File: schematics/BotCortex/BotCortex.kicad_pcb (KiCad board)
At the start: 2 copper layers, 59 parts, among them P1 2x Serial, P10 Stepper Upperarm, P11 Stepper Hip, P12 POWER_IN, P13 PowerEnableIn, P14 Power Stepper 2, P15 Power Stepper 3, P16 Power Stepper 4, P17 PowerEnableOut, P18 Power Stepper 5, P19 ODroid Power, P2 Herkulex Servo, P20 POTI 10K, P21 Reset_Conn, P22 Reset Conn, P23 LED-Driver-I2C, P24 UART6, P25 Thermal_Printer, P28 Power Stepper 1, P3 Encoder Socket 0, P4 Encoder Socket, P5 Stepper Elbow, P6 Power In uC Servo 9V, P7 Power Out uC Servo, P8 Stepper Forearm, P9 Stepper Wrist, Q1 BC237, Q2 BC237, SW2 reset, U1 7805, U2 LM7809ACT, U3 LM7809ACT, U4 Teensy_3.5

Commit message: Started Implementation of Webserver for Odroid
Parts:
- added P26: ResetTaster, Connectors_Molex:Molex_KK_6410-02, F.Cu at (125.7, 68.6)
- moved P21 1.27 mm to (138.4, 68.6)
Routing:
- net Net-(P21-Pad1): track 3.81 -> 14.0 mm
- net GNDPWR: track 709.1 -> 716.7 mm
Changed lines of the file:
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@@
 (kicad_pcb (version 4) (host pcbnew 4.0.2-stable)
   (general
-    (links 136)
+    (links 138)
     (no_connects 14)
     (area 0 0 0 0)
     (thickness 1.6)
     (drawings 4)
-    (tracks 407)
+    (tracks 409)
     (zones 0)
-    (modules 59)
+    (modules 60)
     (nets 53)
   )
@@
   )
   (module Connect:1pin (layer F.Cu)
-    (at 138.43 69.85)
+    (at 138.43 68.58)
     (descr "module 1 pin (ou trou mecanique de percage)")
     (tags DEV)
@@
     )
   )
+  (module Connectors_Molex:Molex_KK_6410-02 (layer F.Cu)
+    (at 125.73 68.58)
+    (descr "Connector Headers with Friction Lock, 22-27-2021, http://www.molex.com/pdm_docs/sd/022272021_sd.pdf")
+    (tags "connector molex kk_6410 22-27-2021")
+    (fp_text reference P26 (at 1 -4.5) (layer F.SilkS)
+      (effects (font (size 1 1) (thickness 0.15)))
+    )
+    (fp_text value ResetTaster (at 1.27 4.5) (layer F.Fab)
+      (effects (font (size 1 1) (thickness 0.15)))
+    )
+    (fp_line (start -1.37 -3.02) (end -1.37 2.98) (layer F.SilkS) (width 0.15))
+    (fp_line (start -1.37 2.98) (end 3.91 2.98) (layer F.SilkS) (width 0.15))
+    (fp_line (start 3.91 2.98) (end 3.91 -3.02) (layer F.SilkS) (width 0.15))
+    (fp_line (start 3.91 -3.02) (end -1.37 -3.02) (layer F.SilkS) (width 0.15))
+    (fp_line (start 0 2.98) (end 0 1.98) (layer F.SilkS) (width 0.15))
+    (fp_line (start 0 1.98) (end 2.54 1.98) (layer F.SilkS) (width 0.15))
+    (fp_line (start 2.54 1.98) (end 2.54 2.98) (layer F.SilkS) (width 0.15))
+    (fp_line (start 0 1.98) (end 0.25 1.55) (layer F.SilkS) (width 0.15))
+    (fp_line (start 0.25 1.55) (end 2.29 1.55) (layer F.SilkS) (width 0.15))
+    (fp_line (start 2.29 1.55) (end 2.54 1.98) (layer F.SilkS) (width 0.15))
+    (fp_line (start 0.25 2.98) (end 0.25 1.98) (layer F.SilkS) (width 0.15))
+    (fp_line (start 2.29 2.98) (end 2.29 1.98) (layer F.SilkS) (width 0.15))
+    (fp_line (start -0.8 -3.02) (end -0.8 -2.4) (layer F.SilkS) (width 0.15))
+    (fp_line (start -0.8 -2.4) (end 0.8 -2.4) (layer F.SilkS) (width 0.15))
+    (fp_line (start 0.8 -2.4) (end 0.8 -3.02) (layer F.SilkS) (width 0.15))
+    (fp_line (start 1.74 -3.02) (end 1.74 -2.4) (layer F.SilkS) (width 0.15))
+    (fp_line (start 1.74 -2.4) (end 3.34 -2.4) (layer F.SilkS) (width 0.15))
+    (fp_line (start 3.34 -2.4) (end 3.34 -3.02) (layer F.SilkS) (width 0.15))
+    (fp_line (start -1.9 3.5) (end -1.9 -3.55) (layer F.CrtYd) (width 0.05))
+    (fp_line (start -1.9 -3.55) (end 4.45 -3.55) (layer F.CrtYd) (width 0.05))
+    (fp_line (start 4.45 -3.55) (end 4.45 3.5) (layer F.CrtYd) (width 0.05))
+    (fp_line (start 4.45 3.5) (end -1.9 3.5) (layer F.CrtYd) (width 0.05))
+    (pad 1 thru_hole rect (at 0 0) (size 2 2.6) (drill 1.2) (layers *.Cu *.Mask F.SilkS)
+      (net 2 GNDPWR))
+    (pad 2 thru_hole oval (at 2.54 0) (size 2 2.6) (drill 1.2) (layers *.Cu *.Mask F.SilkS)
+      (net 44 "Net-(P21-Pad1)"))
+  )
   (target plus (at 91.44 33.02) (size 5) (width 0.1) (layer Edge.Cuts))
   (target plus (at 109.22 125.73) (size 5) (width 0.1) (layer Edge.Cuts))
@@
   (segment (start 182.88 76.2) (end 196.85 76.2) (width 0.25) (layer B.Cu) (net 1) (status 10))
   (segment (start 198.12 73.66) (end 198.12 73.66) (width 0.25) (layer B.Cu) (net 1) (status 30))
+  (segment (start 125.73 68.58) (end 118.11 68.58) (width 0.25) (layer B.Cu) (net 2))
   (segment (start 114.3 111.76) (end 114.3 114.3) (width 0.25) (layer B.Cu) (net 2))
   (segment (start 114.31 114.29) (end 125.74 114.29) (width 0.25) (layer B.Cu) (net 2))
@@
   (segment (start 114.3 83.82) (end 116.84 83.82) (width 0.25) (layer B.Cu) (net 2))
   (segment (start 182.88 109.22) (end 182.88 114.3) (width 0.25) (layer B.Cu) (net 2))
-  (segment (start 205.74 109.22) (end 205.74 114.3) (width 0.25) (layer B.Cu) (net 2))
+  (segment (start 205.74 109.22) (end 205.74 114.3) (width 0.25) (layer B.Cu) (net 2) (status 10))
   (segment (start 205.74 114.3) (end 182.88 114.3) (width 0.25) (layer B.Cu) (net 2))
   (segment (start 205.74 53.34) (end 205.74 45.72) (width 0.25) (layer B.Cu) (net 2))
@@
   (segment (start 205.74 83.82) (end 205.74 73.66) (width 0.25) (layer B.Cu) (net 2) (status 20))
   (segment (start 205.74 93.98) (end 205.74 83.82) (width 0.25) (layer B.Cu) (net 2) (status 20))
-  (segment (start 205.74 93.98) (end 205.74 109.22) (width 0.25) (layer B.Cu) (net 2) (status 10))
+  (segment (start 205.74 93.98) (end 205.74 109.22) (width 0.25) (layer B.Cu) (net 2) (status 20))
   (segment (start 90.17 99.06) (end 92.71 99.06) (width 0.25) (layer B.Cu) (net 2))
   (segment (start 85.09 55.88) (end 78.74 55.88) (width 0.25) (layer B.Cu) (net 2))
@@
   (segment (start 158.75 50.8) (end 167.64 50.8) (width 0.25) (layer B.Cu) (net 33) (status 20))
   (segment (start 182.88 106.68) (end 185.42 106.68) (width 0.25) (layer B.Cu) (net 34))
-  (segment (start 200.66 111.76) (end 200.66 109.22) (width 0.25) (layer B.Cu) (net 34))
+  (segment (start 200.66 111.76) (end 200.66 109.22) (width 0.25) (layer B.Cu) (net 34) (status 20))
   (segment (start 185.42 111.76) (end 200.66 111.76) (width 0.25) (layer B.Cu) (net 34))
   (segment (start 185.42 106.68) (end 185.42 111.76) (width 0.25) (layer B.Cu) (net 34))
   (segment (start 200.66 109.22) (end 200.66 109.22) (width 0.25) (layer B.Cu) (net 34) (status 30))
-  (segment (start 198.12 109.22) (end 187.96 109.22) (width 0.25) (layer B.Cu) (net 35))
+  (segment (start 198.12 109.22) (end 187.96 109.22) (width 0.25) (layer B.Cu) (net 35) (status 10))
   (segment (start 187.96 104.14) (end 182.88 104.14) (width 0.25) (layer B.Cu) (net 35))
   (segment (start 187.96 109.22) (end 187.96 104.14) (width 0.25) (layer B.Cu) (net 35))
@@
   (segment (start 163.83 81.28) (end 167.64 81.28) (width 0.25) (layer B.Cu) (net 43) (status 20))
   (segment (start 163.83 76.2) (end 163.83 81.28) (width 0.25) (layer B.Cu) (net 43))
+  (segment (start 128.27 68.58) (end 138.43 68.58) (width 0.25) (layer B.Cu) (net 44))
   (segment (start 138.43 78.74) (end 138.43 78.74) (width 0.25) (layer B.Cu) (net 44) (status 30))
   (segment (start 125.73 78.74) (end 125.73 78.74) (width 0.25) (layer B.Cu) (net 44) (status 30))
@@
   (segment (start 149.86 48.26) (end 149.86 58.42) (width 0.25) (layer B.Cu) (net 46))
   (segment (start 149.86 58.42) (end 157.48 58.42) (width 0.25) (layer B.Cu) (net 46) (status 20))
-  (segment (start 167.64 104.14) (end 152.4 104.14) (width 0.25) (layer B.Cu) (net 47) (status 400000))
+  (segment (start 167.64 104.14) (end 152.4 104.14) (width 0.25) (layer B.Cu) (net 47))
   (via (at 140.97 81.28) (size 0.6) (drill 0.4) (layers F.Cu B.Cu) (net 47))
   (segment (start 140.97 86.36) (end 140.97 81.28) (width 0.25) (layer F.Cu) (net 47))
@@
   (segment (start 152.4 104.14) (end 147.32 104.14) (width 0.25) (layer F.Cu) (net 47))
   (via (at 152.4 104.14) (size 0.6) (drill 0.4) (layers F.Cu B.Cu) (net 47))
-  (segment (start 140.97 81.28) (end 143.51 81.28) (width 0.25) (layer B.Cu) (net 47) (status 800000))
+  (segment (start 140.97 81.28) (end 143.51 81.28) (width 0.25) (layer B.Cu) (net 47))
   (via (at 157.48 81.28) (size 0.6) (drill 0.4) (layers F.Cu B.Cu) (net 47))
   (segment (start 152.4 81.28) (end 157.48 81.28) (width 0.25) (layer F.Cu) (net 47))

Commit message: no message
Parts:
- P3: value Encoder Socket 0 -> Encoder Socket 1
- P4: value Encoder Socket -> Encoder Socket 0
- moved P23 1.27 mm to (146.1, 48.3)
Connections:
- P23 pad 2: /SCl1 -> /SDA1
- P23 pad 3: /SDA1 -> /SCl1
- U4 pad 29: /SCl1 -> (no net)
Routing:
- net /SCl1: track 38.1 -> 39.4 mm, vias 0 -> 2
- net /+5V: track 151.1 -> 149.9 mm
- net /SDA1: track 47.0 -> 45.7 mm
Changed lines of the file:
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@@
 (kicad_pcb (version 4) (host pcbnew 4.0.2-stable)
   (general
-    (links 138)
+    (links 137)
     (no_connects 14)
     (area 0 0 0 0)
     (thickness 1.6)
     (drawings 4)
-    (tracks 409)
+    (tracks 410)
     (zones 0)
     (modules 60)
@@
       (effects (font (size 1 1) (thickness 0.15)))
     )
-    (fp_text value "Encoder Socket" (at 3.81 4.5 90) (layer F.Fab)
+    (fp_text value "Encoder Socket 0" (at 3.81 4.5 90) (layer F.Fab)
       (effects (font (size 1 1) (thickness 0.15)))
     )
@@
       (effects (font (size 1 1) (thickness 0.15)))
     )
-    (fp_text value "Encoder Socket 0" (at 3.81 4.5 90) (layer F.Fab)
+    (fp_text value "Encoder Socket 1" (at 3.81 4.5 90) (layer F.Fab)
       (effects (font (size 1 1) (thickness 0.15)))
     )
@@
   )
   (module Connectors_Molex:Molex_KK_6410-04 (layer F.Cu)
-    (at 144.78 48.26 180)
+    (at 146.05 48.26 180)
     (descr "Connector Headers with Friction Lock, 22-27-2041, http://www.molex.com/pdm_docs/sd/022272021_sd.pdf")
     (tags "connector molex kk_6410 22-27-2041")
@@
       (net 46 /+5V))
     (pad 2 thru_hole oval (at 2.54 0 180) (size 2 2.6) (drill 1.2) (layers *.Cu *.Mask F.SilkS)
+      (net 36 /SDA1))
+    (pad 3 thru_hole oval (at 5.08 0 180) (size 2 2.6) (drill 1.2) (layers *.Cu *.Mask F.SilkS)
       (net 37 /SCl1))
-    (pad 3 thru_hole oval (at 5.08 0 180) (size 2 2.6) (drill 1.2) (layers *.Cu *.Mask F.SilkS)
-      (net 36 /SDA1))
     (pad 4 thru_hole oval (at 7.62 0 180) (size 2 2.6) (drill 1.2) (layers *.Cu *.Mask F.SilkS)
       (net 2 GNDPWR))
@@
     (pad 27 thru_hole oval (at 15.24 53.34 180) (size 1.6 1.6) (drill 0.8) (layers *.Cu *.Mask F.SilkS))
     (pad 28 thru_hole oval (at 15.24 50.8 180) (size 1.6 1.6) (drill 0.8) (layers *.Cu *.Mask F.SilkS))
-    (pad 29 thru_hole oval (at 15.24 48.26 180) (size 1.6 1.6) (drill 0.8) (layers *.Cu *.Mask F.SilkS)
-      (net 37 /SCl1))
+    (pad 29 thru_hole oval (at 15.24 48.26 180) (size 1.6 1.6) (drill 0.8) (layers *.Cu *.Mask F.SilkS))
     (pad 30 thru_hole oval (at 15.24 45.72 180) (size 1.6 1.6) (drill 0.8) (layers *.Cu *.Mask F.SilkS)
       (net 36 /SDA1))
@@
   (segment (start 182.88 76.2) (end 196.85 76.2) (width 0.25) (layer B.Cu) (net 1) (status 10))
   (segment (start 198.12 73.66) (end 198.12 73.66) (width 0.25) (layer B.Cu) (net 1) (status 30))
+  (segment (start 138.43 48.26) (end 138.43 45.72) (width 0.25) (layer B.Cu) (net 2))
   (segment (start 125.73 68.58) (end 118.11 68.58) (width 0.25) (layer B.Cu) (net 2))
   (segment (start 114.3 111.76) (end 114.3 114.3) (width 0.25) (layer B.Cu) (net 2))
@@
   (segment (start 157.48 73.66) (end 154.94 73.66) (width 0.25) (layer B.Cu) (net 2))
   (segment (start 143.51 91.44) (end 143.51 83.78) (width 0.25) (layer B.Cu) (net 2))
-  (segment (start 137.16 48.26) (end 137.16 45.72) (width 0.25) (layer B.Cu) (net 2))
   (segment (start 114.3 106.68) (end 114.3 111.75) (width 0.25) (layer B.Cu) (net 2))
   (segment (start 114.3 111.75) (end 114.3 111.76) (width 0.25) (layer B.Cu) (net 2))
@@
   (segment (start 138.43 99.02) (end 138.39 99.06) (width 0.25) (layer B.Cu) (net 2))
   (segment (start 151.13 45.72) (end 138.43 45.72) (width 0.25) (layer B.Cu) (net 2))
+  (segment (start 151.13 45.72) (end 152.4 45.72) (width 0.25) (layer B.Cu) (net 2))
   (segment (start 138.43 45.72) (end 137.16 45.72) (width 0.25) (layer B.Cu) (net 2))
   (segment (start 137.16 45.72) (end 135.89 45.72) (width 0.25) (layer B.Cu) (net 2))
@@
   (segment (start 116.88 106.72) (end 116.84 106.68) (width 0.25) (layer B.Cu) (net 2) (status 30))
   (segment (start 152.4 45.72) (end 205.74 45.72) (width 0.25) (layer B.Cu) (net 2))
-  (segment (start 151.13 45.72) (end 152.4 45.72) (width 0.25) (layer B.Cu) (net 2))
   (segment (start 205.74 63.5) (end 205.74 53.34) (width 0.25) (layer B.Cu) (net 2) (status 20))
   (segment (start 205.74 73.66) (end 205.74 63.5) (width 0.25) (layer B.Cu) (net 2) (status 20))
@@
   (segment (start 187.96 104.14) (end 182.88 104.14) (width 0.25) (layer B.Cu) (net 35))
   (segment (start 187.96 109.22) (end 187.96 104.14) (width 0.25) (layer B.Cu) (net 35))
-  (segment (start 139.7 48.26) (end 139.7 58.42) (width 0.25) (layer B.Cu) (net 36))
-  (segment (start 144.78 58.42) (end 144.78 63.5) (width 0.25) (layer B.Cu) (net 36))
-  (segment (start 139.7 58.42) (end 144.78 58.42) (width 0.25) (layer B.Cu) (net 36))
-  (segment (start 151.13 63.5) (end 144.78 63.5) (width 0.25) (layer B.Cu) (net 36))
+  (segment (start 143.51 48.26) (end 143.51 63.5) (width 0.25) (layer B.Cu) (net 36) (status 400000))
+  (segment (start 152.4 63.5) (end 151.13 63.5) (width 0.25) (layer B.Cu) (net 36) (status 800000))
+  (segment (start 143.51 63.5) (end 152.4 63.5) (width 0.25) (layer B.Cu) (net 36))
   (segment (start 157.48 63.5) (end 171.45 63.5) (width 0.25) (layer B.Cu) (net 36) (status 10))
   (segment (start 151.13 63.5) (end 157.48 63.5) (width 0.25) (layer B.Cu) (net 36) (status 20))
-  (segment (start 142.24 48.26) (end 142.24 55.88) (width 0.25) (layer B.Cu) (net 37))
-  (segment (start 147.32 60.96) (end 151.13 60.96) (width 0.25) (layer B.Cu) (net 37))
-  (segment (start 147.32 55.88) (end 147.32 60.96) (width 0.25) (layer B.Cu) (net 37))
-  (segment (start 142.24 55.88) (end 147.32 55.88) (width 0.25) (layer B.Cu) (net 37))
+  (segment (start 151.13 60.96) (end 146.05 60.96) (width 0.25) (layer B.Cu) (net 37) (status 400000))
+  (segment (start 140.97 53.34) (end 140.97 48.26) (width 0.25) (layer B.Cu) (net 37) (status 800000))
+  (via (at 140.97 53.34) (size 0.6) (drill 0.4) (layers F.Cu B.Cu) (net 37))
+  (segment (start 146.05 53.34) (end 140.97 53.34) (width 0.25) (layer F.Cu) (net 37))
+  (via (at 146.05 53.34) (size 0.6) (drill 0.4) (layers F.Cu B.Cu) (net 37))
+  (segment (start 146.05 60.96) (end 146.05 53.34) (width 0.25) (layer B.Cu) (net 37))
+  (segment (start 151.13 60.96) (end 157.48 60.96) (width 0.25) (layer B.Cu) (net 37) (status 20))
   (segment (start 167.64 60.96) (end 163.83 60.96) (width 0.25) (layer B.Cu) (net 37) (status 10))
   (segment (start 163.83 60.96) (end 157.48 60.96) (width 0.25) (layer B.Cu) (net 37) (status 20))
-  (segment (start 151.13 60.96) (end 157.48 60.96) (width 0.25) (layer B.Cu) (net 37) (status 20))
   (segment (start 157.48 91.44) (end 161.29 91.44) (width 0.25) (layer B.Cu) (net 38))
   (segment (start 162.56 88.9) (end 167.64 88.9) (width 0.25) (layer B.Cu) (net 38))
@@
   (segment (start 152.4 109.22) (end 167.64 109.22) (width 0.25) (layer B.Cu) (net 46) (status 20))
   (segment (start 138.43 109.22) (end 116.84 109.22) (width 0.25) (layer B.Cu) (net 46) (status 20))
-  (segment (start 144.78 48.26) (end 149.86 48.26) (width 0.25) (layer B.Cu) (net 46))
+  (segment (start 146.05 48.26) (end 149.86 48.26) (width 0.25) (layer B.Cu) (net 46) (status 10))
   (segment (start 149.86 48.26) (end 149.86 58.42) (width 0.25) (layer B.Cu) (net 46))
   (segment (start 149.86 58.42) (end 157.48 58.42) (width 0.25) (layer B.Cu) (net 46) (status 20))

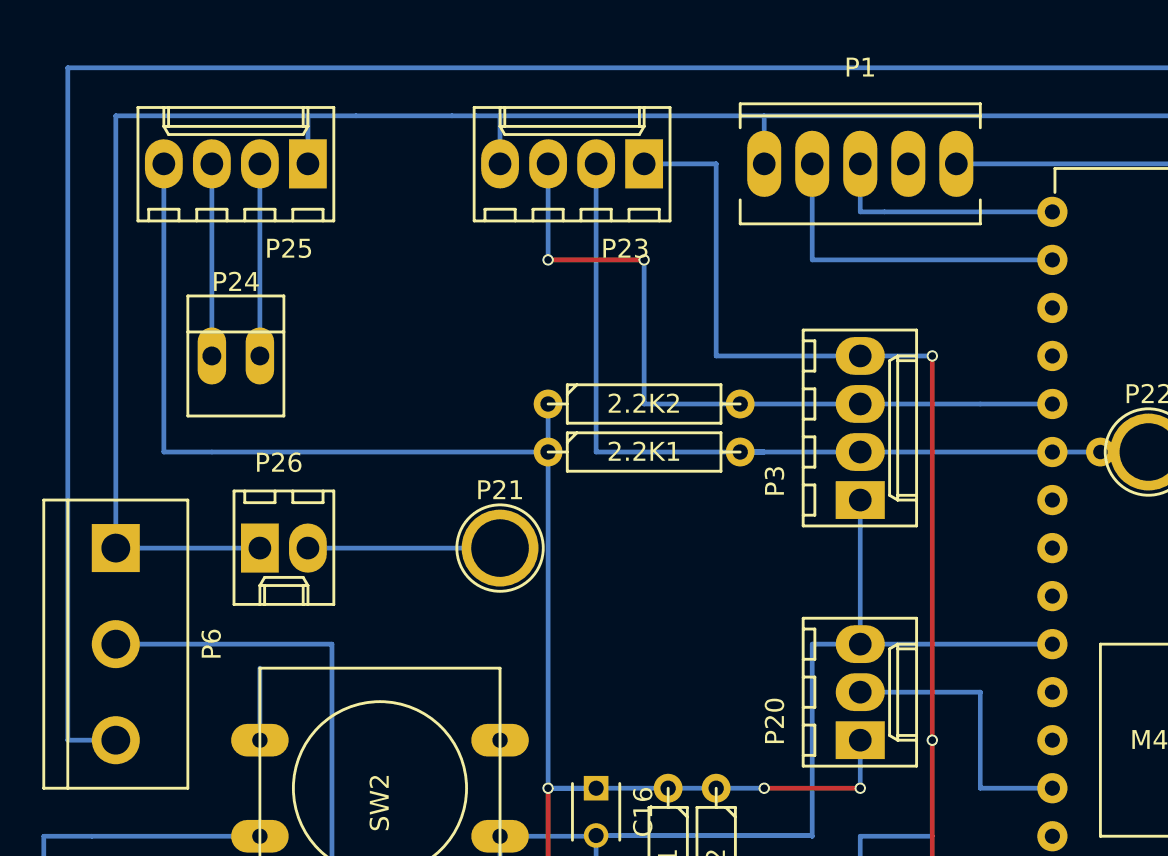
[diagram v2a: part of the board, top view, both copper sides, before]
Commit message: added Reset LED to schematics and Cortex
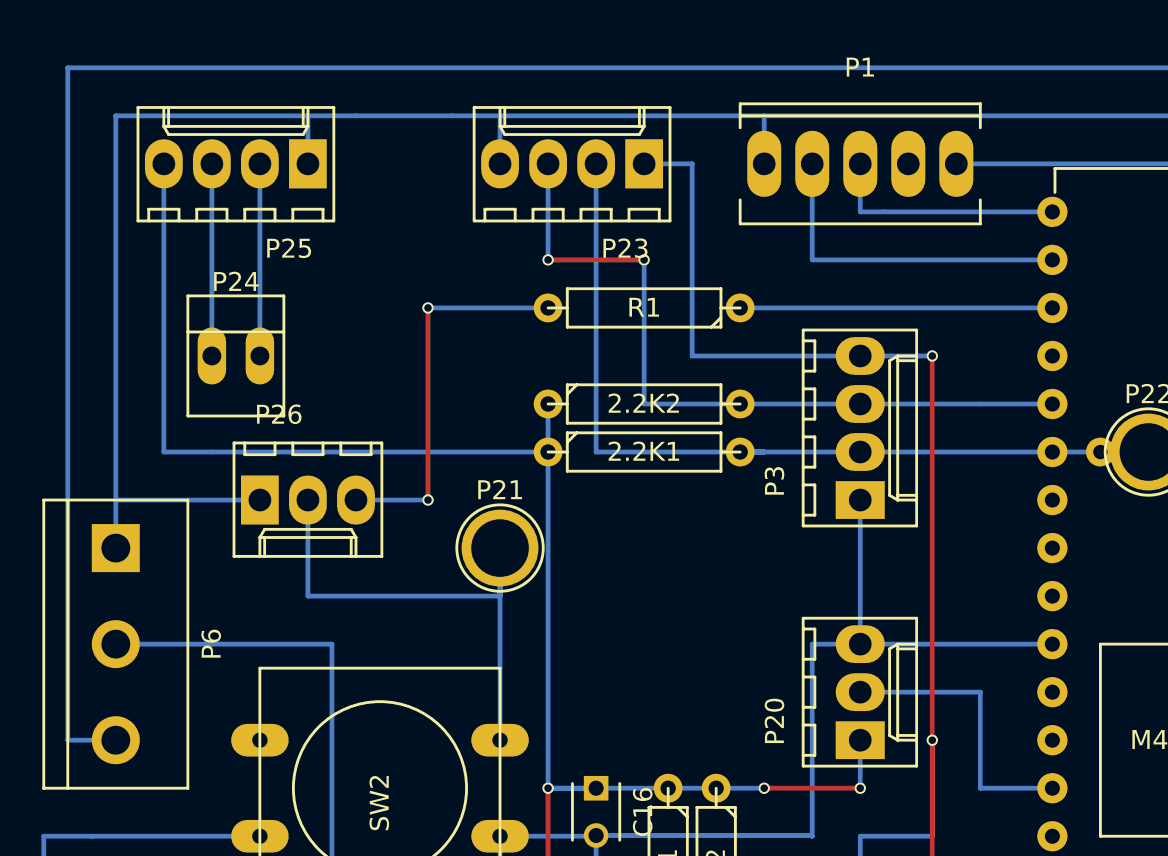
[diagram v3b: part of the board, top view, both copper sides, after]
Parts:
- added R1: 220, Discret:R4, F.Cu at (146.1, 55.9)
- P26: value ResetTaster -> Reset Anschluss; footprint Connectors_Molex:Molex_KK_6410-02 -> Connectors_Molex:Molex_KK_6410-03
- moved P26 2.54 mm to (125.7, 66.0)
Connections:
- net Net-(P21-Pad1) renamed /RESET
- U4 pad 27: (no net) -> Net-(R1-Pad1)
- U4 pad 29: (no net) -> /SCl1
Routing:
- net /Reset-LED: track 0.00 -> 20.3 mm, vias 0 -> 2
- net Net-(R1-Pad1): track 0.00 -> 16.5 mm
- net /RESET: track 14.0 -> 27.9 mm
